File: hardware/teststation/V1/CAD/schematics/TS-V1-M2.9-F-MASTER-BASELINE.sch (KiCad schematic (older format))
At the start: 0 parts

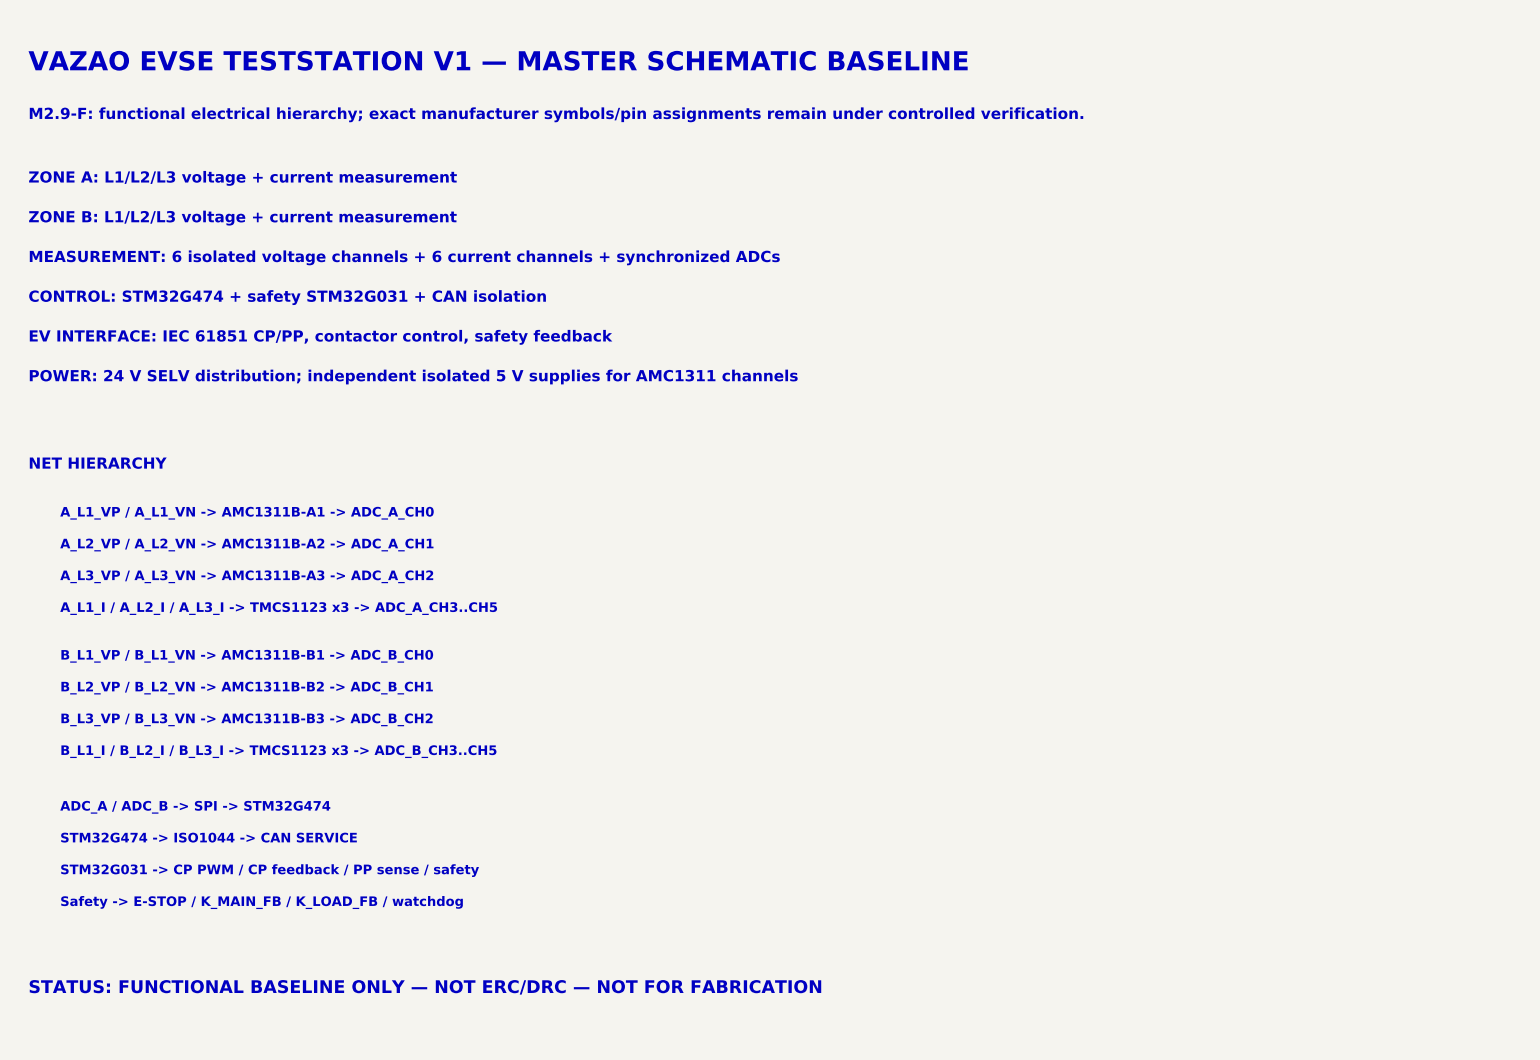
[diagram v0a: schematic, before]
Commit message: feat(teststation): instantiate M2.9-G schematic components
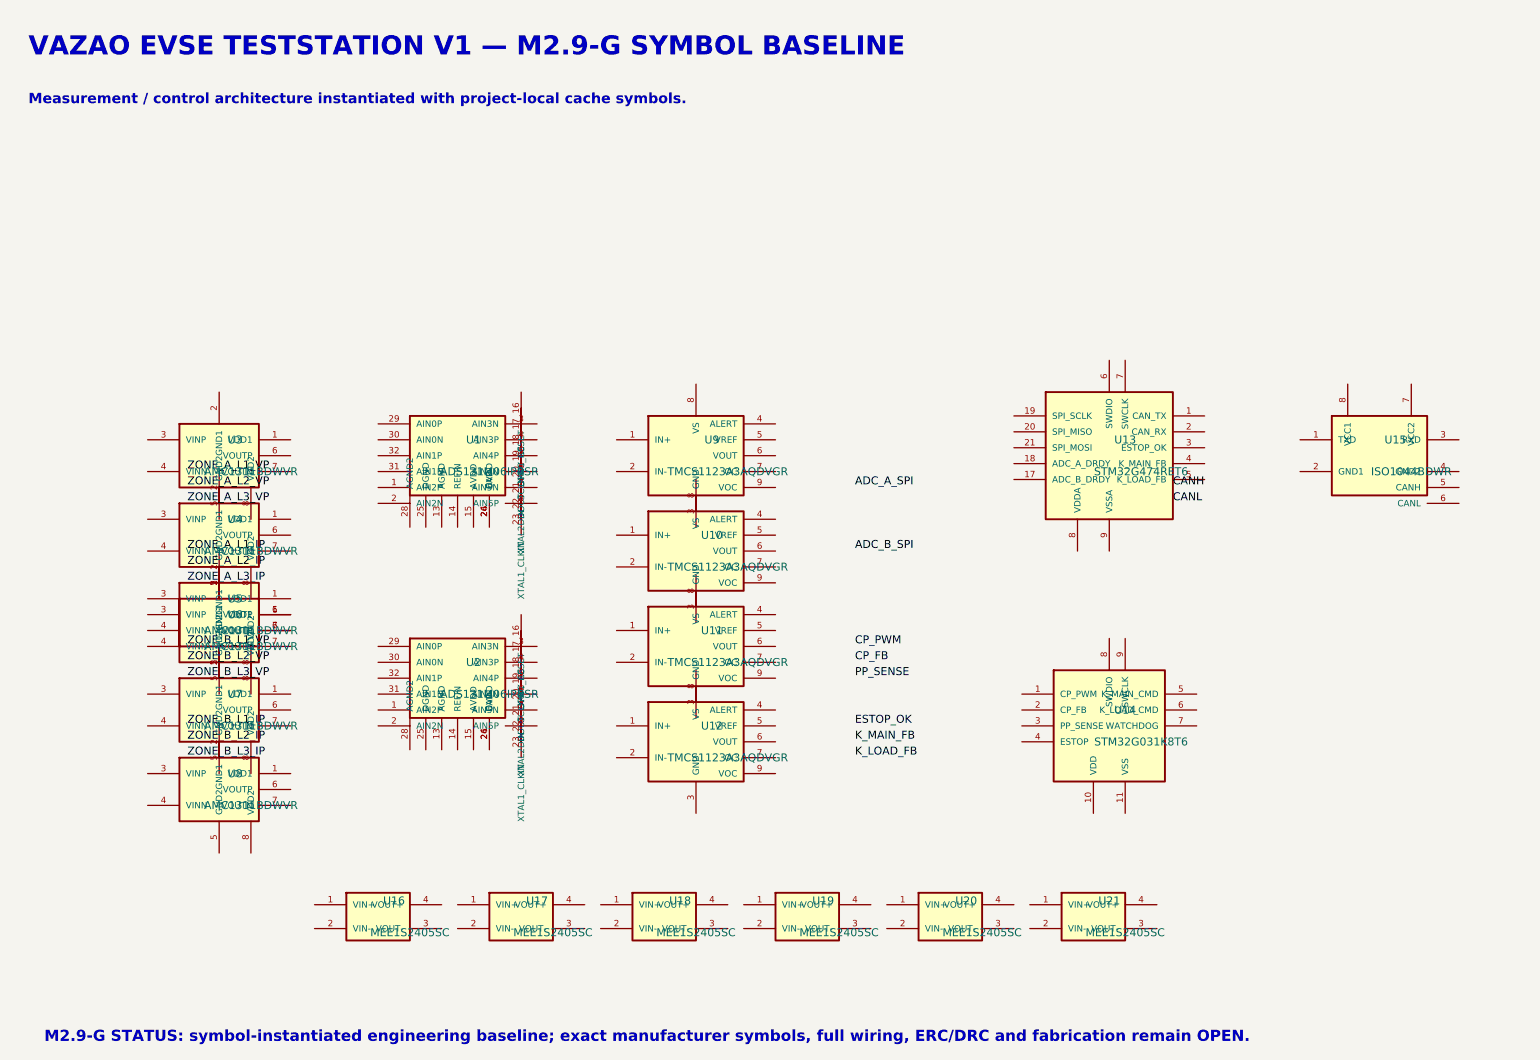
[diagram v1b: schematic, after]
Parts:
- added U1, U2: ADS131M06IPBSR, symbol ADS131M06IPBSR
- added U10, U11, U12, U9: TMCS1123A3AQDVGR, symbol TMCS1123A3AQDVGR
- added U13: STM32G474RET6, symbol STM32G474RET6
- added U14: STM32G031K8T6, symbol STM32G031K8T6
- added U15: ISO1044BDWR, symbol ISO1044BDWR
- added U16, U17, U18, U19, U20, U21: MEE1S2405SC, symbol MEE1S2405SC
- added U3, U4, U5, U6, U7, U8: AMC1311BDWVR, symbol AMC1311BDWVR
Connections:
- new net: U1.24 (CAP), U1.26 (DVDD)
- new net: U2.24 (CAP), U2.26 (DVDD)
- new net: U5.6 (VOUTP), U6.1 (VDD1)
- new net: U5.7 (VOUTN), U6.6 (VOUTP)
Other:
- note added: "M2.9-G STATUS: symbol-instantiated engineering baseline; exact manufacturer symbols, full wiring, ERC/DRC and fabrication remain OPEN."
- note added: "Measurement / control architecture instantiated with project-local cache symbols."
- note added: "VAZAO EVSE TESTSTATION V1 — M2.9-G SYMBOL BASELINE"
- note removed: "ADC_A / ADC_B -> SPI -> STM32G474"
- note removed: "A_L1_I / A_L2_I / A_L3_I -> TMCS1123 x3 -> ADC_A_CH3..CH5"
- note removed: "A_L1_VP / A_L1_VN -> AMC1311B-A1 -> ADC_A_CH0"
- note removed: "A_L2_VP / A_L2_VN -> AMC1311B-A2 -> ADC_A_CH1"
- note removed: "A_L3_VP / A_L3_VN -> AMC1311B-A3 -> ADC_A_CH2"
- note removed: "B_L1_I / B_L2_I / B_L3_I -> TMCS1123 x3 -> ADC_B_CH3..CH5"
- note removed: "B_L1_VP / B_L1_VN -> AMC1311B-B1 -> ADC_B_CH0"
- note removed: "B_L2_VP / B_L2_VN -> AMC1311B-B2 -> ADC_B_CH1"
- note removed: "B_L3_VP / B_L3_VN -> AMC1311B-B3 -> ADC_B_CH2"
- note removed: "CONTROL: STM32G474 + safety STM32G031 + CAN isolation"
- note removed: "EV INTERFACE: IEC 61851 CP/PP, contactor control, safety feedback"
- note removed: "M2.9-F: functional electrical hierarchy; exact manufacturer symbols/pin assignments remain under controlled verification."
- note removed: "MEASUREMENT: 6 isolated voltage channels + 6 current channels + synchronized ADCs"
- note removed: "NET HIERARCHY"
- note removed: "POWER: 24 V SELV distribution; independent isolated 5 V supplies for AMC1311 channels"
- note removed: "STATUS: FUNCTIONAL BASELINE ONLY — NOT ERC/DRC — NOT FOR FABRICATION"
- note removed: "STM32G031 -> CP PWM / CP feedback / PP sense / safety"
- note removed: "STM32G474 -> ISO1044 -> CAN SERVICE"
- note removed: "Safety -> E-STOP / K_MAIN_FB / K_LOAD_FB / watchdog"
- note removed: "VAZAO EVSE TESTSTATION V1 — MASTER SCHEMATIC BASELINE"
- note removed: "ZONE A: L1/L2/L3 voltage + current measurement"
- note removed: "ZONE B: L1/L2/L3 voltage + current measurement"

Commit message: feat(teststation): update schematic connectivity baseline M2.9-H
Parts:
- removed U1, U2: ADS131M06IPBSR, symbol ADS131M06IPBSR
- removed U10, U11, U12, U9: TMCS1123A3AQDVGR, symbol TMCS1123A3AQDVGR
- removed U13: STM32G474RET6, symbol STM32G474RET6
- removed U14: STM32G031K8T6, symbol STM32G031K8T6
- removed U15: ISO1044BDWR, symbol ISO1044BDWR
- removed U16, U17, U18, U19, U20, U21: MEE1S2405SC, symbol MEE1S2405SC
- removed U3, U4, U5, U6, U7, U8: AMC1311BDWVR, symbol AMC1311BDWVR
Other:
- note added: "ADC CONTROL: ADC_A/B SPI + DRDY + SYNC/RESET -> STM32G474"
- note added: "CAN: STM32G474 -> ISO1044 -> CANH/CANL"
- note added: "DECOUPLING: local ceramic bypass at every IC supply; final values follow exact manufacturer recommendations."
- note added: "EV CONTROL: STM32G031 -> CP_PWM / CP_FB / PP_SENSE / contactor commands"
- note added: "ISOLATION: 24V_SELV -> MEE1S2405SC x6 -> independent ISO_5V_x / ISO_GND_x"
- note added: "M2.9-H STATUS: CONNECTIVITY CONTRACT — NOT ERC CLEAN — NOT DRC CLEAN — NOT FOR FABRICATION"
- note added: "POWER: 24V input protection -> 24V distribution -> 3.3V measurement/control rails"
- note added: "SAFETY: E-STOP -> independent energy removal + ESTOP_OK / K_MAIN_FB / K_LOAD_FB"
- note added: "VAZAO EVSE TESTSTATION V1 — M2.9-H CONNECTIVITY BASELINE"
- note added: "ZONE A CURRENT: A_L1_I/A_L2_I/A_L3_I -> TMCS1123-A1/A2/A3 -> ADC_A_CH3..CH5"
- note added: "ZONE A VOLTAGE: A_L1_VP/A_L1_VN -> AMC1311-A1 -> ADC_A_CH0"
- note added: "ZONE A VOLTAGE: A_L2_VP/A_L2_VN -> AMC1311-A2 -> ADC_A_CH1"
- note added: "ZONE A VOLTAGE: A_L3_VP/A_L3_VN -> AMC1311-A3 -> ADC_A_CH2"
- note added: "ZONE A/B measurement, isolated supplies, ADC SPI, MCU control, CAN isolation, CP/PP and safety nets."
- note added: "ZONE B CURRENT: B_L1_I/B_L2_I/B_L3_I -> TMCS1123-B1/B2/B3 -> ADC_B_CH3..CH5"
- note added: "ZONE B VOLTAGE: B_L1/B_L2/B_L3 -> AMC1311-B1/B2/B3 -> ADC_B_CH0..CH2"
- note removed: "M2.9-G STATUS: symbol-instantiated engineering baseline; exact manufacturer symbols, full wiring, ERC/DRC and fabrication remain OPEN."
- note removed: "Measurement / control architecture instantiated with project-local cache symbols."
- note removed: "VAZAO EVSE TESTSTATION V1 — M2.9-G SYMBOL BASELINE"

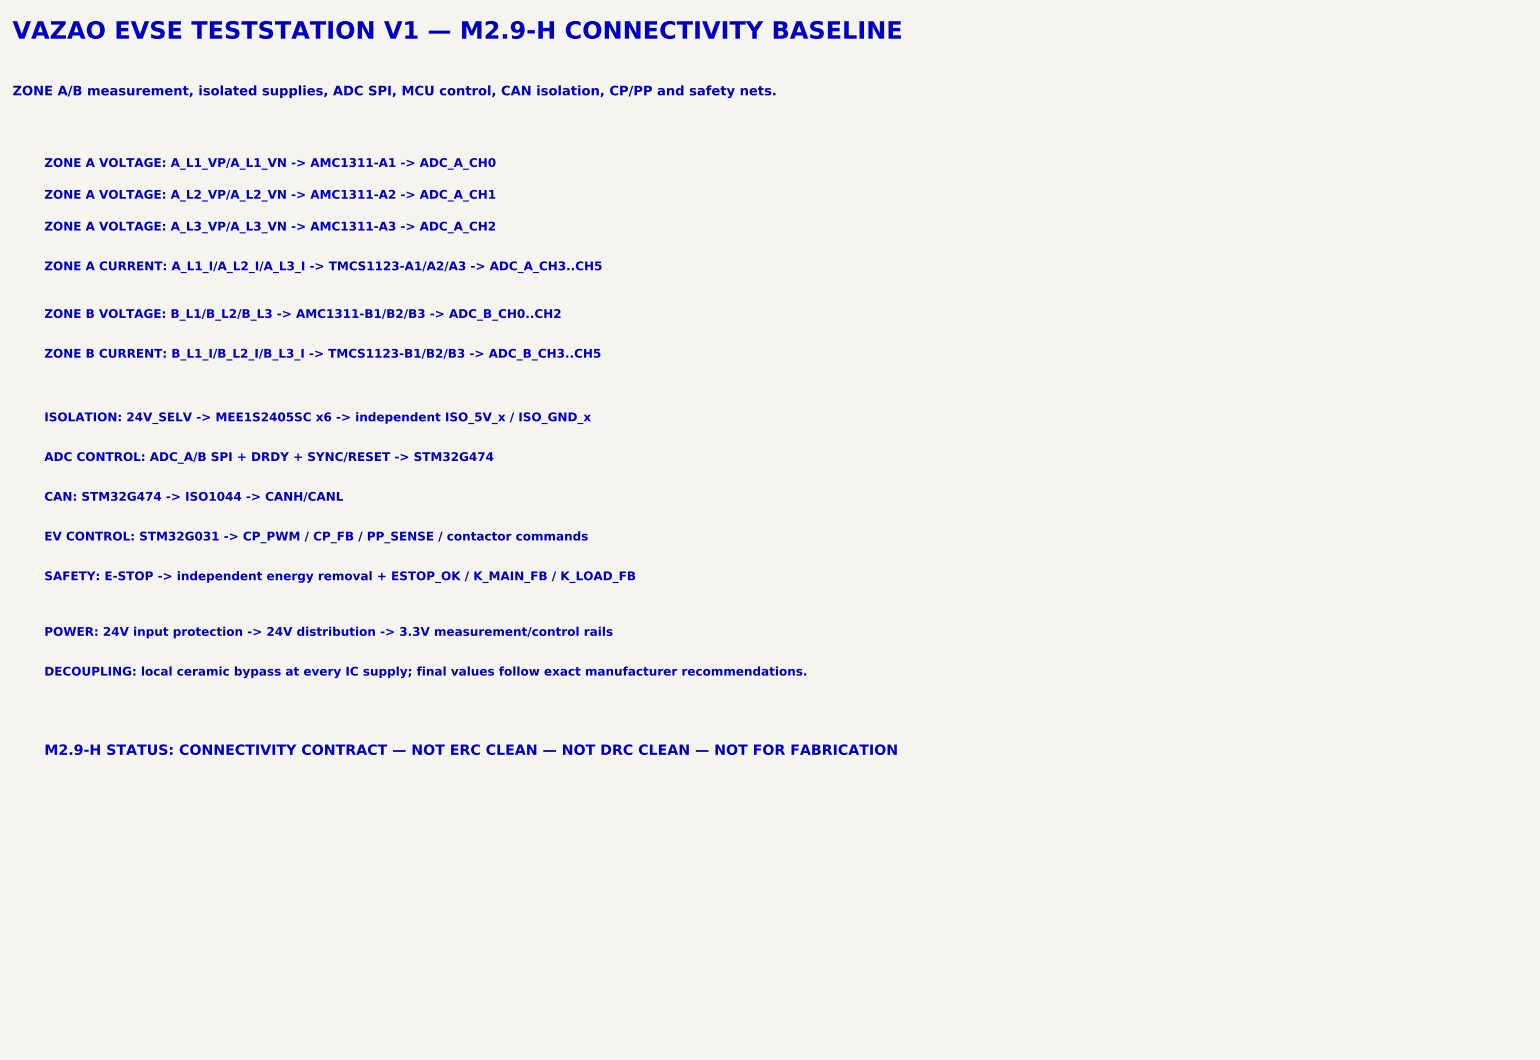
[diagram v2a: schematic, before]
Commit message: Advance TestStation schematic baseline to M2.9-I
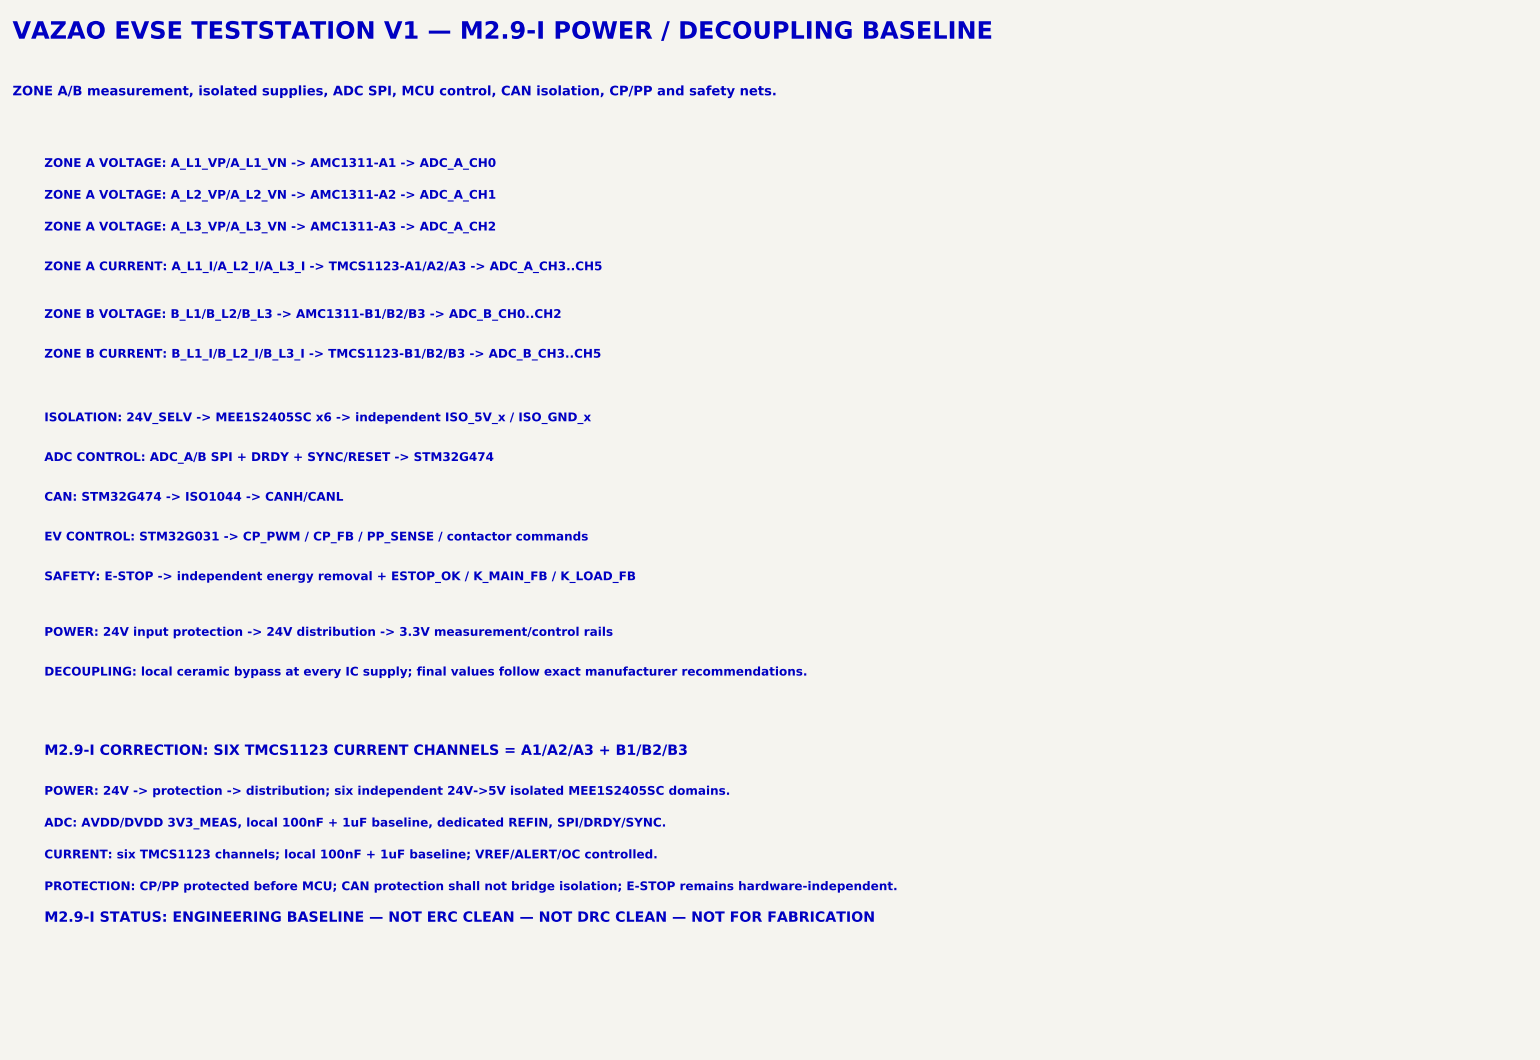
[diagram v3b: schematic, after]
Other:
- note added: "ADC: AVDD/DVDD 3V3_MEAS, local 100nF + 1uF baseline, dedicated REFIN, SPI/DRDY/SYNC."
- note added: "CURRENT: six TMCS1123 channels; local 100nF + 1uF baseline; VREF/ALERT/OC controlled."
- note added: "M2.9-I CORRECTION: SIX TMCS1123 CURRENT CHANNELS = A1/A2/A3 + B1/B2/B3"
- note added: "M2.9-I STATUS: ENGINEERING BASELINE — NOT ERC CLEAN — NOT DRC CLEAN — NOT FOR FABRICATION"
- note added: "POWER: 24V -> protection -> distribution; six independent 24V->5V isolated MEE1S2405SC domains."
- note added: "PROTECTION: CP/PP protected before MCU; CAN protection shall not bridge isolation; E-STOP remains hardware-independent."
- note added: "VAZAO EVSE TESTSTATION V1 — M2.9-I POWER / DECOUPLING BASELINE"
- note removed: "M2.9-H STATUS: CONNECTIVITY CONTRACT — NOT ERC CLEAN — NOT DRC CLEAN — NOT FOR FABRICATION"
- note removed: "VAZAO EVSE TESTSTATION V1 — M2.9-H CONNECTIVITY BASELINE"
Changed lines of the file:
@@
 Title "VAZAO EVSE TestStation V1"
 Date "2026-09-26"
-Rev "M2.9-H"
+Rev "M2.9-I"
 Comp "VAZAO EVSE"
-Comment1 "Connected-net and power baseline"
+Comment1 "Power, decoupling and protection baseline"
 Comment2 "NO MAINS ENERGIZATION"
 Comment3 "ERC/DRC pending"
-Comment4 "M2.9-H"
+Comment4 "M2.9-I"
 $EndDescr
 Text Notes 700 700 0 110 ~ 22
-VAZAO EVSE TESTSTATION V1 — M2.9-H CONNECTIVITY BASELINE
+VAZAO EVSE TESTSTATION V1 — M2.9-I POWER / DECOUPLING BASELINE
 Text Notes 700 1050 0 60 ~ 12
 ZONE A/B measurement, isolated supplies, ADC SPI, MCU control, CAN isolation, CP/PP and safety nets.
@@
 DECOUPLING: local ceramic bypass at every IC supply; final values follow exact manufacturer recommendations.
 Text Notes 900 5200 0 65 ~ 13
-M2.9-H STATUS: CONNECTIVITY CONTRACT — NOT ERC CLEAN — NOT DRC CLEAN — NOT FOR FABRICATION
+M2.9-I CORRECTION: SIX TMCS1123 CURRENT CHANNELS = A1/A2/A3 + B1/B2/B3
+Text Notes 900 5450 0 55 ~ 11
+POWER: 24V -> protection -> distribution; six independent 24V->5V isolated MEE1S2405SC domains.
+Text Notes 900 5650 0 55 ~ 11
+ADC: AVDD/DVDD 3V3_MEAS, local 100nF + 1uF baseline, dedicated REFIN, SPI/DRDY/SYNC.
+Text Notes 900 5850 0 55 ~ 11
+CURRENT: six TMCS1123 channels; local 100nF + 1uF baseline; VREF/ALERT/OC controlled.
+Text Notes 900 6050 0 55 ~ 11
+PROTECTION: CP/PP protected before MCU; CAN protection shall not bridge isolation; E-STOP remains hardware-independent.
+Text Notes 900 6250 0 65 ~ 13
+M2.9-I STATUS: ENGINEERING BASELINE — NOT ERC CLEAN — NOT DRC CLEAN — NOT FOR FABRICATION
 $EndSCHEMATC
